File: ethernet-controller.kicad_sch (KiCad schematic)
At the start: 39 parts, among them J1 5-2337992-8, U1 RTL8111H, Y1 ABM8G-25.000MHZ-18-D2Y-T

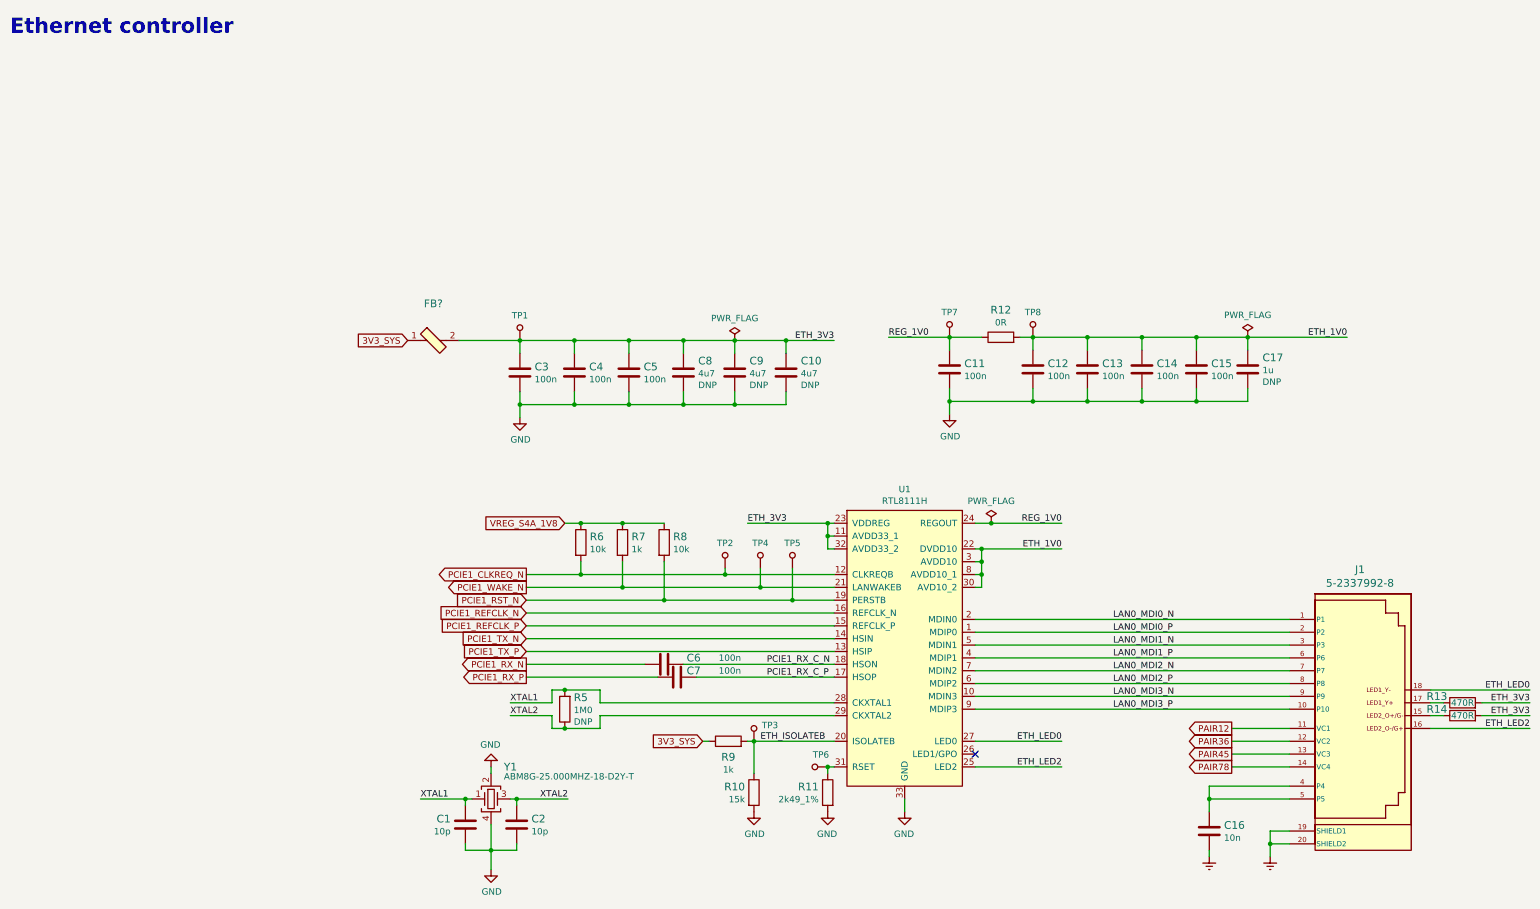
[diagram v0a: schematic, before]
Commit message: Introduce component standardization
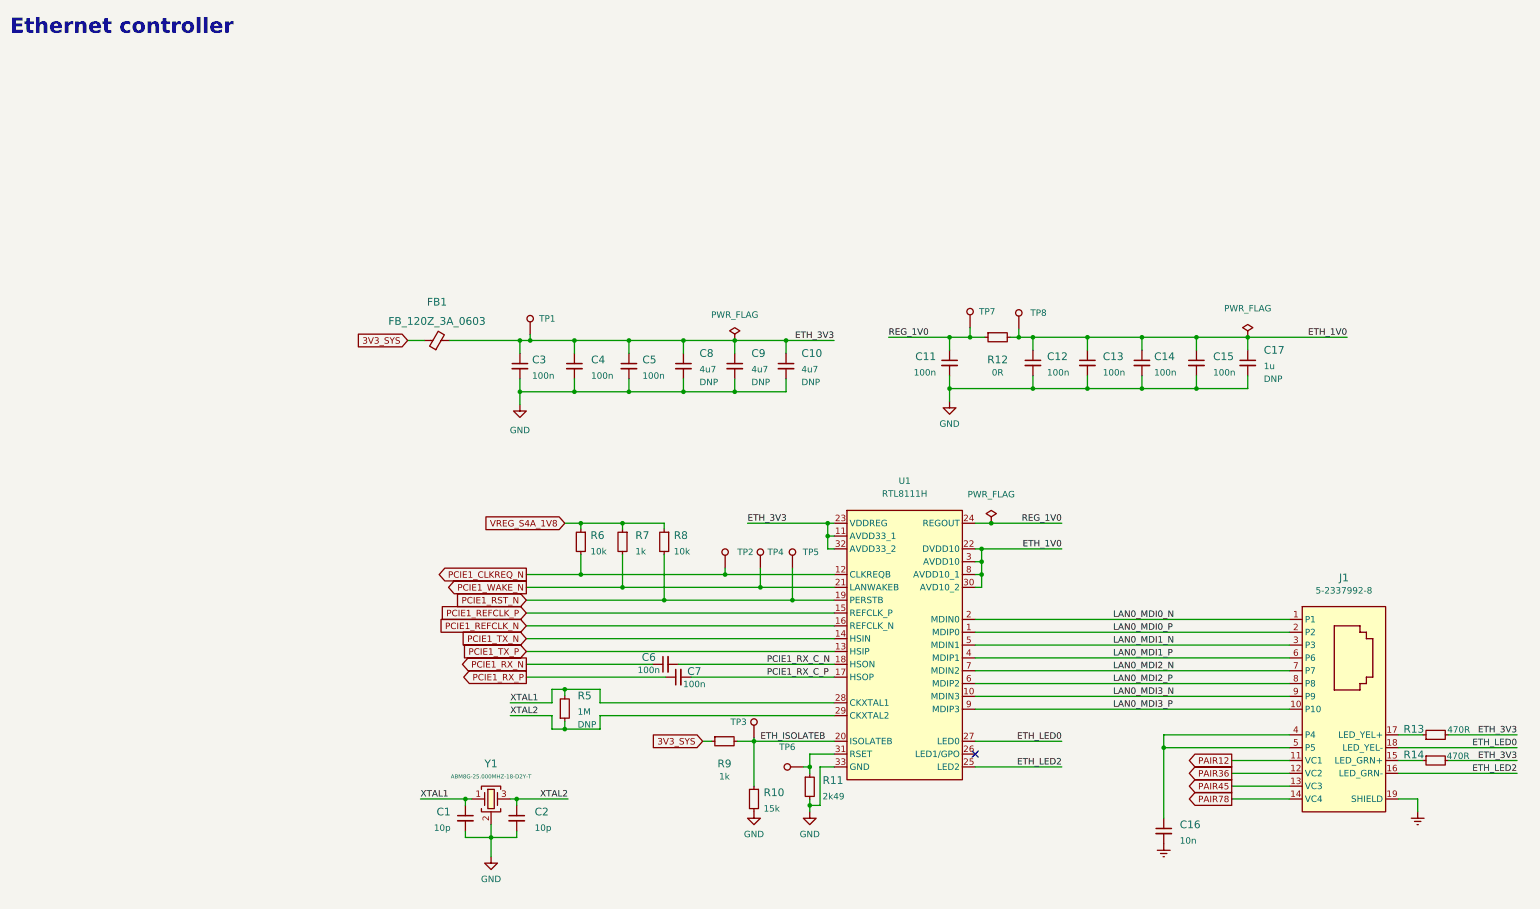
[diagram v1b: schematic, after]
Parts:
- C1, C2: footprint sa800u-baseboard-hw-footprints:0402-cap -> sa800u-baseboard-hw-footprints:C_0402_1005Metric; Author (none) -> Antmicro; Dielectric (none) -> C0G; License (none) -> Apache-2.0; MPN MC0402N100D500CT -> GCM1555C1H100GA16D; Manufacturer MULTICOMP -> Murata; Voltage (none) -> 50V
- C10, C8, C9: footprint sa800u-baseboard-hw-footprints:0402-cap -> sa800u-baseboard-hw-footprints:C_0402_1005Metric; Author (none) -> Antmicro; License (none) -> Apache-2.0; Manufacturer MURATA -> Murata
- C11, C12, C13, C14, C15, C3, C4, C5, C6, C7: footprint sa800u-baseboard-hw-footprints:0402-cap -> sa800u-baseboard-hw-footprints:C_0402_1005Metric; Author (none) -> Antmicro; Dielectric (none) -> X5R; License (none) -> Apache-2.0; MPN 0402X104K6R3CT -> GRM155R61H104KE14D; Manufacturer Walsin -> Murata; Voltage (none) -> 50V
- C16: footprint sa800u-baseboard-hw-footprints:0402-cap -> sa800u-baseboard-hw-footprints:C_0402_1005Metric; Author (none) -> Antmicro; Dielectric (none) -> X7R; License (none) -> Apache-2.0; MPN 04025G103ZAT2A -> GRM155R71H103KA88D; Manufacturer AVX -> Murata; Voltage (none) -> 50V
- C17: footprint sa800u-baseboard-hw-footprints:0402-cap -> sa800u-baseboard-hw-footprints:C_0402_1005Metric; Author (none) -> Antmicro; License (none) -> Apache-2.0
- FB1: renamed from FB?; value (none) -> FB_120Z_3A_0603; footprint (none) -> sa800u-baseboard-hw-footprints:FB_0603_1608Metric; symbol sa800u-baseboard-hw:BLM18SG121TN1D -> sa800u-baseboard-hw:FB_120Z_3A_0603; Author (none) -> Antmicro; License (none) -> Apache-2.0; Manufacturer Murata Electronics North America -> Murata
- J1: value 5-2337992-8 -> Bus_RJ45_5-2337992-8; footprint sa800u-baseboard-hw-footprints:5-2337992-8 -> sa800u-baseboard-hw-footprints:RJ45_5-2337992-8_Horizontal; symbol sa800u-baseboard-hw:5-2337992-8 -> sa800u-baseboard-hw:Bus_RJ45_5-2337992-8; Author (none) -> Antmicro; License (none) -> Apache-2.0
- R10: footprint sa800u-baseboard-hw-footprints:0603-res -> sa800u-baseboard-hw-footprints:R_0603_1608Metric; Author (none) -> Antmicro; License (none) -> Apache-2.0; Manufacturer BOURNS -> Bourns; Tolerance (none) -> 1%
- R11: value R_2k49_1%_0402 -> R_2k49_0402; footprint sa800u-baseboard-hw-footprints:0402-res -> sa800u-baseboard-hw-footprints:R_0402_1005Metric; symbol sa800u-baseboard-hw:R_2k49_1%_0402 -> sa800u-baseboard-hw:R_2k49_0402; Author (none) -> Antmicro; License (none) -> Apache-2.0; MPN CR0502-FX-2491GLF -> CR0402-FX-2491GLF; Tolerance (none) -> 1%; Val 2k49_1% -> 2k49
- R12: footprint sa800u-baseboard-hw-footprints:0402-res -> sa800u-baseboard-hw-footprints:R_0402_1005Metric; Author (none) -> Antmicro; Current (none) -> 1A; License (none) -> Apache-2.0; Manufacturer PANASONIC -> Panasonic
- R13, R14: footprint sa800u-baseboard-hw-footprints:0402-res -> sa800u-baseboard-hw-footprints:R_0402_1005Metric; Author (none) -> Antmicro; License (none) -> Apache-2.0; MPN CRCW0402470RFKED -> CR0402-FX-4700GLF; Manufacturer VISHAY -> Bourns; Tolerance (none) -> 1%
- R5: value R_1M0_0402 -> R_1M_0402; footprint sa800u-baseboard-hw-footprints:0402-res -> sa800u-baseboard-hw-footprints:R_0402_1005Metric; symbol sa800u-baseboard-hw:R_1M0_0402 -> sa800u-baseboard-hw:R_1M_0402; Author (none) -> Antmicro; License (none) -> Apache-2.0; MPN CRG0402F1M0 -> CR0402-FX-1004GLF; Manufacturer TE CONNECTIVITY -> Bourns; Tolerance (none) -> 1%; Val 1M0 -> 1M
- R6, R8: footprint sa800u-baseboard-hw-footprints:0402-res -> sa800u-baseboard-hw-footprints:R_0402_1005Metric; Author (none) -> Antmicro; License (none) -> Apache-2.0; MPN CRCW040210K0FKEDHP -> CR0402-FX-1002GLF; Manufacturer VISHAY -> Bourns; Tolerance (none) -> 1%
- R7, R9: footprint sa800u-baseboard-hw-footprints:0402-res -> sa800u-baseboard-hw-footprints:R_0402_1005Metric; Author (none) -> Antmicro; License (none) -> Apache-2.0; Manufacturer BOURNS -> Bourns; Tolerance (none) -> 1%
- TP1, TP2, TP3, TP4, TP5, TP6, TP7, TP8: value TP_SMD_0_75MM -> TP_0.75mm_SMD; footprint sa800u-baseboard-hw-footprints:Testpoint_smd_0_75mm -> sa800u-baseboard-hw-footprints:TP_SMD_0.75mm; symbol sa800u-baseboard-hw:TP_SMD_0_75MM -> sa800u-baseboard-hw:TP_0.75mm_SMD; Author (none) -> Antmicro; License (none) -> Apache-2.0
- U1: footprint sa800u-baseboard-hw-footprints:RTL8111H -> sa800u-baseboard-hw-footprints:QFN-32-1EP_4x4mm_P0.4mm; Author (none) -> Antmicro; License (none) -> Apache-2.0; Manufacturer REALTEK -> Realtek
- Y1: value ABM8G-25.000MHZ-18-D2Y-T -> Oscillator_SMD_25MHz_KX-7; footprint sa800u-baseboard-hw-footprints:KX-7 -> sa800u-baseboard-hw-footprints:Oscillator_SMD_Geyer_KX-7-4Pin_3.2x2.5mm; symbol sa800u-baseboard-hw:ABM8G-25.000MHZ-18-D2Y-T -> sa800u-baseboard-hw:Oscillator_SMD_25MHz_KX-7; Author (none) -> Antmicro; License (none) -> Apache-2.0; Val (none) -> 25MHz
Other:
- moved on the sheet: C1, C10, C11, C12, C13, C14, C15, C16, C17, C2, C3, C4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

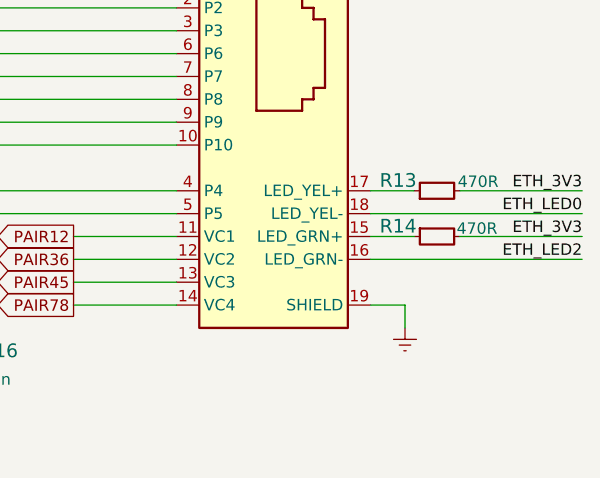
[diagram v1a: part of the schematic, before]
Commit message: Add OHP assets
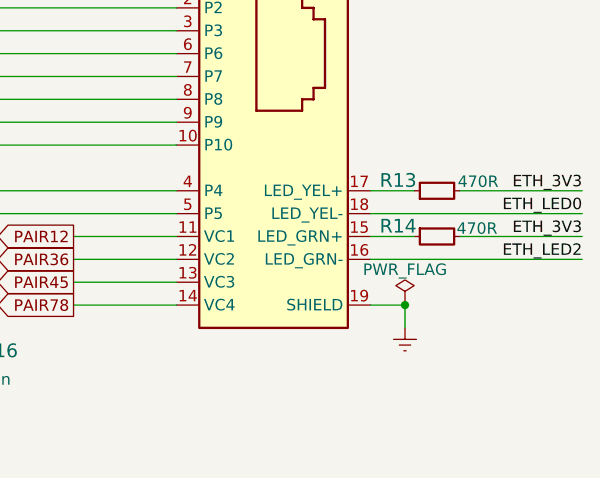
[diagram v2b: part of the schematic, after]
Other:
- company: (none) -> Antmicro Ltd.
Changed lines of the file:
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@@
   (title_block
     (title "SA800U (Snapdragon 845) Baseboard")
-    (date "2023-07-27")
-    (rev "1.0.2")
+    (date "2023-10-19")
+    (rev "1.0.3")
+    (company "Antmicro Ltd.")
     (comment 1 "www.antmicro.com")
-    (comment 2 "Antmicro Ltd.")
   )
   (junction (at 108.585 177.165) (diameter 0) (color 0 0 0 0)
@@
   (junction (at 207.645 114.935) (diameter 0) (color 0 0 0 0)
   )
+  (junction (at 292.1 169.545) (diameter 0) (color 0 0 0 0)
+  )
   (junction (at 215.9 78.105) (diameter 0) (color 0 0 0 0)
   )
@@
     (stroke (width 0) (type default) (color 0 0 0 0))
   )
+  (wire (pts (xy 292.1 169.291) (xy 292.1 169.545))
+    (stroke (width 0) (type default) (color 0 0 0 0))
+  )
   (wire (pts (xy 134.62 127.635) (xy 161.925 127.635))
     (stroke (width 0) (type default) (color 0 0 0 0))
@@
       (effects (font (size 1.27 1.27)) hide)
     )
+    (pin "1")
+  )
+  (symbol (lib_id "sa800u-baseboard-hw:PWR_FLAG") (at 292.1 169.291 0) (unit 1)
+    (in_bom yes) (on_board yes)
+    (property "Reference" "#FLG028" (id 0) (at 292.1 167.386 0)
+      (effects (font (size 1.27 1.27)) hide)
+    )
+    (property "Value" "PWR_FLAG" (id 1) (at 292.1 165.608 0))
+    (property "Footprint" "" (id 2) (at 292.1 169.291 0)
+      (effects (font (size 1.27 1.27)) hide)
+    )
+    (property "Datasheet" "~" (id 3) (at 292.1 169.291 0)
+      (effects (font (size 1.27 1.27)) hide)
+    )
